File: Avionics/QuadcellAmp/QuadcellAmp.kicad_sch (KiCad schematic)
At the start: 1 part

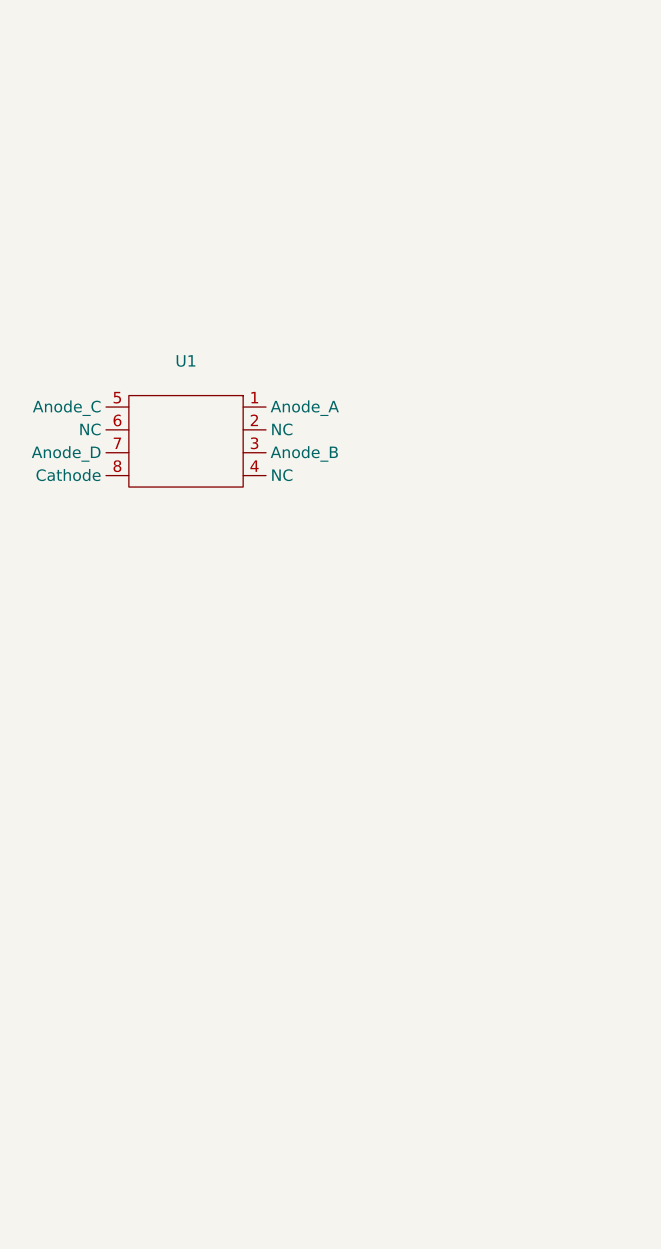
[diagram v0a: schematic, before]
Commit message: circuits build, need review and finalized data to calculate specs
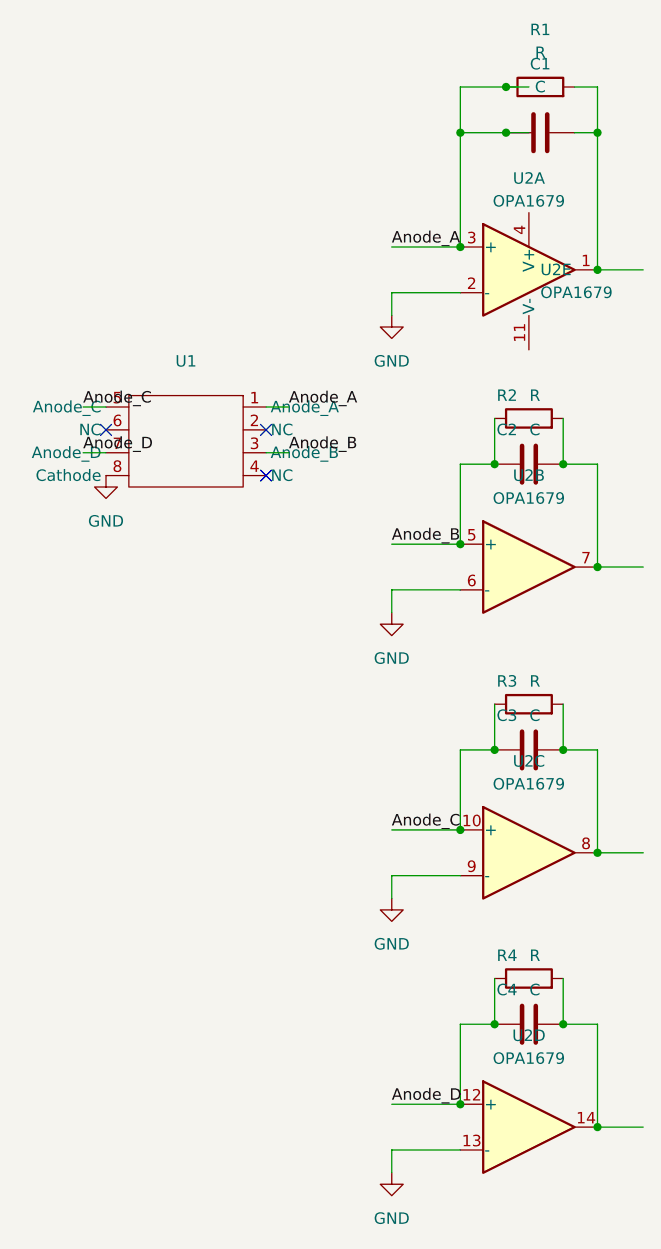
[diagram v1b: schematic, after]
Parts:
- added C1, C2, C3, C4: C, symbol Device:C
- added R1, R2, R3, R4: R, symbol Device:R
- added U2: OPA1679, symbol Amplifier_Operational:OPA1679
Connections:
- new net: C4.2, R4.2, U2.14
- new net: C2.2, R2.2, U2.7
- new net: C1.2, R1.2, U2.1
- new net: C3.2, R3.2, U2.8
- new net Anode_A: C1.1, R1.1, U2.3 (+)
- new net Anode_B: C2.1, R2.1, U2.5 (+)
- new net Anode_C: C3.1, R3.1, U2.10 (+)
- new net Anode_D: C4.1, R4.1, U2.12 (+)
- new net GND: U2.13 (-), U2.2 (-), U2.6 (-), U2.9 (-)
- no-connect marks 0 -> 3

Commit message: Finished Quadcell Amp v1.0
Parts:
- C1, C2, C3, C4: footprint (none) -> Capacitor_THT:CP_Axial_L10.0mm_D4.5mm_P15.00mm_Horizontal
- R1, R2, R3, R4: footprint (none) -> Resistor_THT:R_Axial_DIN0204_L3.6mm_D1.6mm_P1.90mm_Vertical
- U1: footprint (none) -> Library:Quadcell
- U2: footprint (none) -> Package_DIP:DIP-14_W7.62mm
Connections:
- net Anode_A: now also U1.8 (Anode_A)
- net Anode_B: now also U1.6 (Anode_B)
- net Anode_C: now also U1.4 (Anode_C)
- net Anode_D: now also U1.2 (Anode_D)
- net GND: now also U1.1 (Cathode)
- net V_NEG: now reaches U2.11 (V-)
- net V_POS: now reaches U2.4 (V+)
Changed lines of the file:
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@@
+	)
+	(junction
+		(at 134.62 73.66)
+		(diameter 0)
+		(color 0 0 0 0)
 	)
 	(junction
@@
 	)
 	(junction
-		(at 134.62 73.66)
-		(diameter 0)
-		(color 0 0 0 0)
-	)
-	(junction
 		(at 149.86 171.45)
 		(diameter 0)
@@
 	)
 	(no_connect
-		(at 95.25 93.98)
+		(at 118.11 96.52)
 	)
 	(no_connect
-		(at 113.03 99.06)
+		(at 90.17 91.44)
 	)
 	(no_connect
-		(at 113.03 93.98)
+		(at 90.17 96.52)
 	)
 	(wire
@@
 	(wire
 		(pts
-			(xy 92.71 91.44) (xy 95.25 91.44)
+			(xy 142.24 68.58) (xy 142.24 69.85)
+		)
+		(stroke
+			(width 0)
+			(type default)
+		)
+	)
+	(wire
+		(pts
+			(xy 127 73.66) (xy 134.62 73.66)
+		)
+		(stroke
+			(width 0)
+			(type default)
+		)
+	)
+	(wire
+		(pts
+			(xy 118.11 91.44) (xy 124.46 91.44)
 		)
 		(stroke
@@
 	(wire
 		(pts
-			(xy 113.03 96.52) (xy 115.57 96.52)
+			(xy 118.11 99.06) (xy 120.65 99.06)
 		)
 		(stroke
@@
 	(wire
 		(pts
+			(xy 86.36 93.98) (xy 90.17 93.98)
+		)
+		(stroke
+			(width 0)
+			(type default)
+		)
+	)
+	(wire
+		(pts
 			(xy 134.62 129.54) (xy 134.62 138.43)
 		)
@@
 	(wire
 		(pts
-			(xy 92.71 96.52) (xy 95.25 96.52)
+			(xy 118.11 93.98) (xy 120.65 93.98)
 		)
 		(stroke
@@
 	(wire
 		(pts
+			(xy 142.24 85.09) (xy 142.24 86.36)
+		)
+		(stroke
+			(width 0)
+			(type default)
+		)
+	)
+	(wire
+		(pts
 			(xy 142.24 60.96) (xy 139.7 60.96)
 		)
@@
 	(wire
 		(pts
-			(xy 127 73.66) (xy 134.62 73.66)
-		)
-		(stroke
-			(width 0)
-			(type default)
-		)
-	)
-	(wire
-		(pts
 			(xy 138.43 92.71) (xy 138.43 97.79)
 		)
@@
 	(wire
 		(pts
+			(xy 86.36 99.06) (xy 90.17 99.06)
+		)
+		(stroke
+			(width 0)
+			(type default)
+		)
+	)
+	(wire
+		(pts
 			(xy 134.62 143.51) (xy 127 143.51)
 		)
@@
 		(pts
 			(xy 127 106.68) (xy 134.62 106.68)
-		)
-		(stroke
-			(width 0)
-			(type default)
-		)
-	)
-	(wire
-		(pts
-			(xy 113.03 91.44) (xy 115.57 91.44)
 		)
 		(stroke
@@
 		)
 	)
-	(label "Anode_B"
-		(at 127 106.68 0)
+	(label "V_POS"
+		(at 142.24 68.58 0)
 		(fields_autoplaced yes)
 		(effects
@@
 	)
 	(label "Anode_B"
-		(at 115.57 96.52 0)
+		(at 127 106.68 0)
 		(fields_autoplaced yes)
 		(effects
@@
 		)
 	)
-	(label "Anode_A"
-		(at 115.57 91.44 0)
+	(label "V_NEG"
+		(at 142.24 86.36 0)
 		(fields_autoplaced yes)
 		(effects
@@
 		)
 	)
-	(label "Anode_C"
-		(at 92.71 91.44 0)
+	(label "Anode_A"
+		(at 86.36 99.06 0)
 		(fields_autoplaced yes)
 		(effects
@@
 		)
 	)
-	(label "Anode_D"
-		(at 92.71 96.52 0)
+	(label "Anode_B"
+		(at 86.36 93.98 0)
 		(fields_autoplaced yes)
 		(effects
@@
 		)
 	)
-	(label "Anode_D"
-		(at 127 168.91 0)
+	(label "Anode_C"
+		(at 120.65 99.06 0)
 		(fields_autoplaced yes)
 		(effects
@@
 		)
 	)
+	(label "Anode_D"
+		(at 127 168.91 0)
+		(fields_autoplaced yes)
+		(effects
+			(font
+				(size 1.27 1.27)
+			)
+			(justify left bottom)
+		)
+	)
+	(label "Anode_D"
+		(at 120.65 93.98 0)
+		(fields_autoplaced yes)
+		(effects
+			(font
+				(size 1.27 1.27)
+			)
+			(justify left bottom)
+		)
+	)
 	(symbol
 		(lib_id "power:GND")
-		(at 95.25 99.06 0)
+		(at 124.46 91.44 0)
 		(unit 1)
 		(exclude_from_sim no)
@@
 		(fields_autoplaced yes)
 		(property "Reference" "#PWR05"
-			(at 95.25 105.41 0)
+			(at 124.46 97.79 0)
 			(effects
 				(font
@@
 		)
 		(property "Value" "GND"
-			(at 95.25 104.14 0)
+			(at 124.46 96.52 0)
 			(effects
 				(font
@@
 		)
 		(property "Footprint" ""
-			(at 95.25 99.06 0)
+			(at 124.46 91.44 0)
 			(effects
 				(font
@@
 		)
 		(property "Datasheet" ""
-			(at 95.25 99.06 0)
+			(at 124.46 91.44 0)
 			(effects
 				(font
@@
 		)
 		(property "Description" "Power symbol creates a global label with name \"GND\" , ground"
-			(at 95.25 99.06 0)
+			(at 124.46 91.44 0)
 			(effects
 				(font
@@
 			)
 		)
-		(property "Footprint" ""
+		(property "Footprint" "Resistor_THT:R_Axial_DIN0204_L3.6mm_D1.6mm_P1.90mm_Vertical"
 			(at 142.24 156.718 90)
 			(effects
@@
 			)
 		)
-		(property "Footprint" ""
+		(property "Footprint" "Capacitor_THT:CP_Axial_L10.0mm_D4.5mm_P15.00mm_Horizontal"
 			(at 146.05 159.0548 0)
 			(effects
@@
 			)
 		)
-		(property "Footprint" ""
+		(property "Footprint" "Package_DIP:DIP-14_W7.62mm"
 			(at 143.51 74.93 0)
 			(effects
@@
 			)
 		)
-		(property "Footprint" ""
+		(property "Footprint" "Capacitor_THT:CP_Axial_L10.0mm_D4.5mm_P15.00mm_Horizontal"
 			(at 146.05 96.8248 0)
 			(effects
@@
 			)
 		)
-		(property "Footprint" ""
+		(property "Footprint" "Library:Quadcell"
 			(at 104.14 96.52 0)
 			(effects
@@
 			)
 		)
-		(property "Footprint" ""
+		(property "Footprint" "Capacitor_THT:CP_Axial_L10.0mm_D4.5mm_P15.00mm_Horizontal"
 			(at 147.32 59.9948 0)
 			(effects
@@
 			)
 		)
-		(property "Footprint" ""
+		(property "Footprint" "Resistor_THT:R_Axial_DIN0204_L3.6mm_D1.6mm_P1.90mm_Vertical"
 			(at 142.24 126.238 90)
 			(effects
@@
 			)
 		)
-		(property "Footprint" ""
+		(property "Footprint" "Resistor_THT:R_Axial_DIN0204_L3.6mm_D1.6mm_P1.90mm_Vertical"
 			(at 142.24 94.488 90)
 			(effects
@@
 			)
 		)
-		(property "Footprint" ""
+		(property "Footprint" "Package_DIP:DIP-14_W7.62mm"
 			(at 140.97 73.66 0)
 			(effects
@@
 			)
 		)
-		(property "Footprint" ""
+		(property "Footprint" "Package_DIP:DIP-14_W7.62mm"
 			(at 140.97 106.68 0)
 			(effects
@@
 			)
 		)
-		(property "Footprint" ""
+		(property "Footprint" "Capacitor_THT:CP_Axial_L10.0mm_D4.5mm_P15.00mm_Horizontal"
 			(at 146.05 128.5748 0)
 			(effects
@@
 			)
 		)
-		(property "Footprint" ""
+		(property "Footprint" "Package_DIP:DIP-14_W7.62mm"
 			(at 140.97 138.43 0)
 			(effects
@@
 			)
 		)
-		(property "Footprint" ""
+		(property "Footprint" "Resistor_THT:R_Axial_DIN0204_L3.6mm_D1.6mm_P1.90mm_Vertical"
 			(at 143.51 57.658 90)
 			(effects
@@
 			)
 		)
-		(property "Footprint" ""
+		(property "Footprint" "Package_DIP:DIP-14_W7.62mm"
 			(at 140.97 168.91 0)
 			(effects
